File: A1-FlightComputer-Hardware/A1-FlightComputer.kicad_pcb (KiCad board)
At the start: 4 copper layers, 74.8 x 74.8 mm, 86 parts, among them J203 Conn_01x02_Socket, J204 Conn_01x02_Socket, J205 Conn_02x05_Odd_Even, J301 Conn_01x02_Socket, J302 Conn_01x02_Socket, J401 PWR_IN, J402 USB_B_Micro, Q301 Q_NMOS_GSD, SW201 SW_Push, SW202 SW_Push, SW203 SW_SPDT, SW401 SW_SPST, U201 STM32L475RCTx, U202 W25N01GVZEIG, U301 BMP390, U302 LSM6DSOTR, U303 ADXL314, U401 AZ1117-5.0, U402 AZ1117-3.3, Y201 32.768kHz LSE, Y202 8MHz HSE

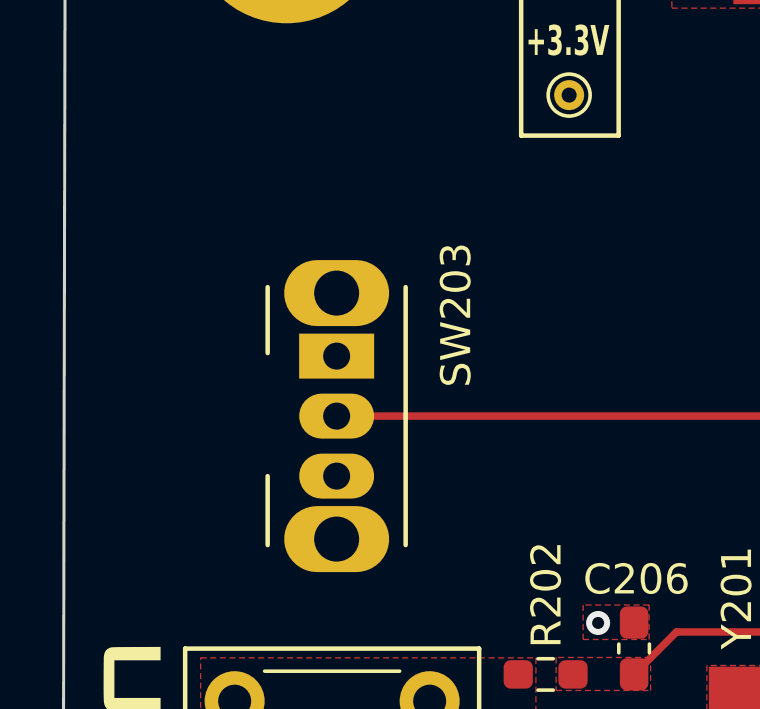
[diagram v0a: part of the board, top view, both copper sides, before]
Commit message: Added better labelling to boo0 switch
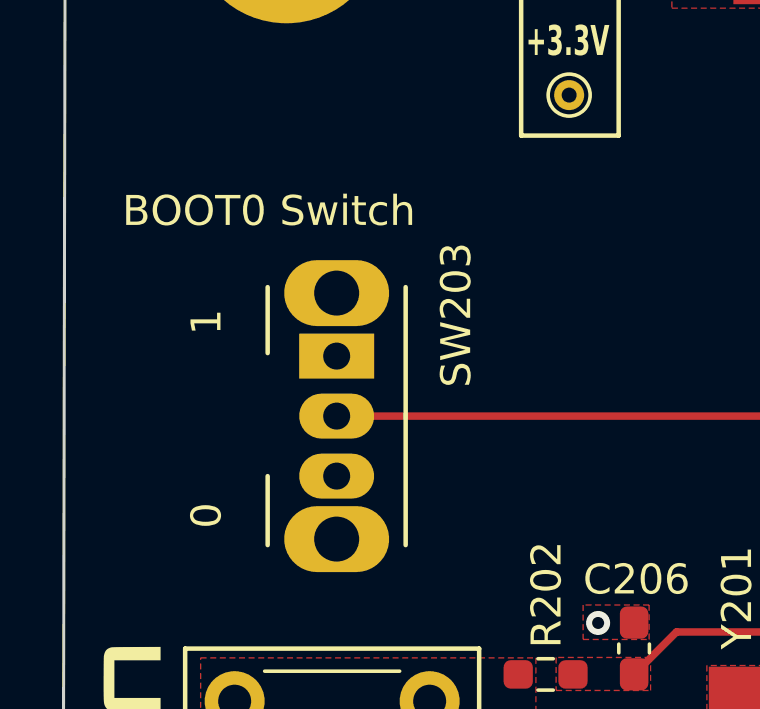
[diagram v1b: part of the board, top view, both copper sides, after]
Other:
- board text added: "0"
- board text added: "1"
- board text added: "BOOT0 Switch"
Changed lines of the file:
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@@
+		)
+	)
+	(gr_text "1"
+		(at 125.6 62.85 90)
+		(layer "F.SilkS")
+		(effects
+			(font
+				(size 1 1)
+				(thickness 0.15)
+			)
+			(justify left bottom)
 		)
 	)
@@
 		)
 	)
+	(gr_text "0"
+		(at 125.6 69.3 90)
+		(layer "F.SilkS")
+		(effects
+			(font
+				(size 1 1)
+				(thickness 0.15)
+			)
+			(justify left bottom)
+		)
+	)
 	(gr_text "+3.3V"
 		(at 137.05 53.05 0)
@@
 		)
 	)
+	(gr_text "BOOT0 Switch"
+		(at 122.2 59.3 0)
+		(layer "F.SilkS")
+		(effects
+			(font
+				(size 1 1)
+				(thickness 0.15)
+			)
+			(justify left bottom)
+		)
+	)

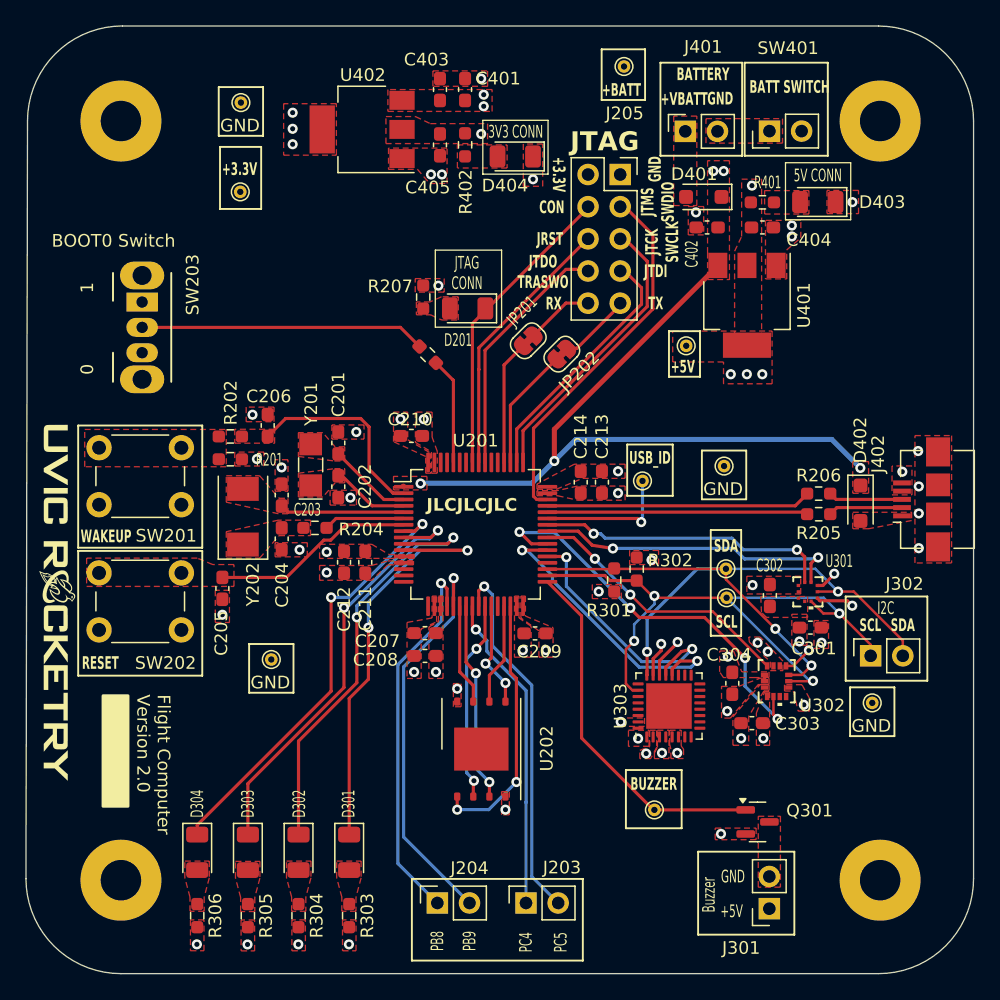
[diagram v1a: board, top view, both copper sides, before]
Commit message: Added voltage divider and connected BATT+ to ADC pin, spaced out battery and switch ports
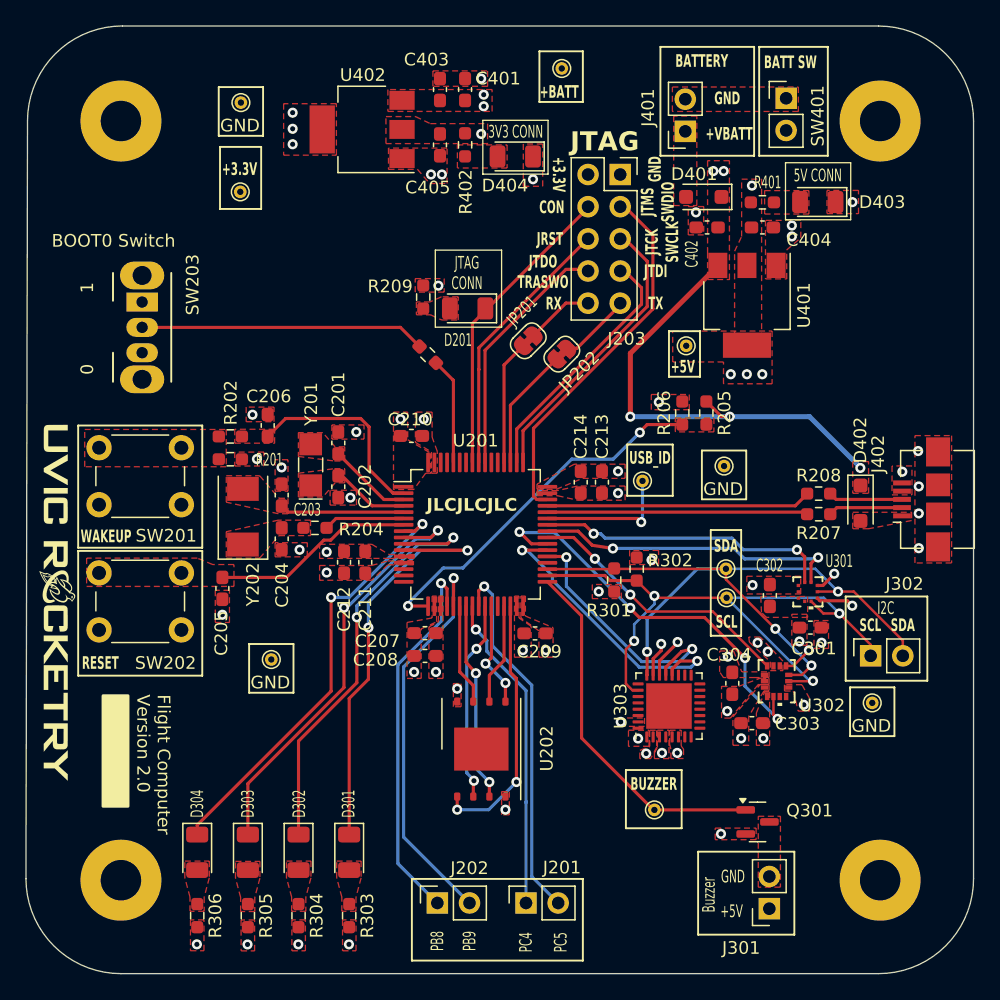
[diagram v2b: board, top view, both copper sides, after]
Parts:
- added R205: 240R, Resistor_SMD:R_0603_1608Metric_Pad0.98x0.95mm_HandSolder, F.Cu at (173.9, 72.3)
- added R206: 240R, Resistor_SMD:R_0603_1608Metric_Pad0.98x0.95mm_HandSolder, F.Cu at (172.0, 72.3)
- moved TP401 4.92 mm to (162.5, 45.1)
- moved SW401 2.91 mm to (180.2, 47.5), turned to 0 degrees
- turned J401 to 180 degrees
- renumbered J203 to J201, J204 to J202, J205 to J203, R205 to R207, R206 to R208, R207 to R209
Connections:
- U201 pad 1: +BATT -> +3V3
- U201 pad 17: unconnected-(U201-PA3-Pad17) -> Net-(U201-PA3)
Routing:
- net Net-(U201-PA3): track 0.00 -> 29.3 mm, vias 0 -> 2
- net +BATT: track 57.9 -> 37.0 mm
- net GND: vias 37 -> 38
- added copper zone on F.Cu, net Net-(U201-PA3)
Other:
- board text added: "BATT SW"
- board text removed: "BATT SWITCH"
